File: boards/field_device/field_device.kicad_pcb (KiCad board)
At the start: 4 copper layers, 35 x 43.9 mm, 54 parts, among them J1 Conn_01x05_Pin, J2 Conn_01x02_Pin, SW1 SW_SPST, U1 CHT20MEMS, U2 STM32C011F6Px, U3 SPA06-003, U4 CN3163, U6 SX1262IMLTRT, U7 TPS63900, Y1 Crystal_GND24

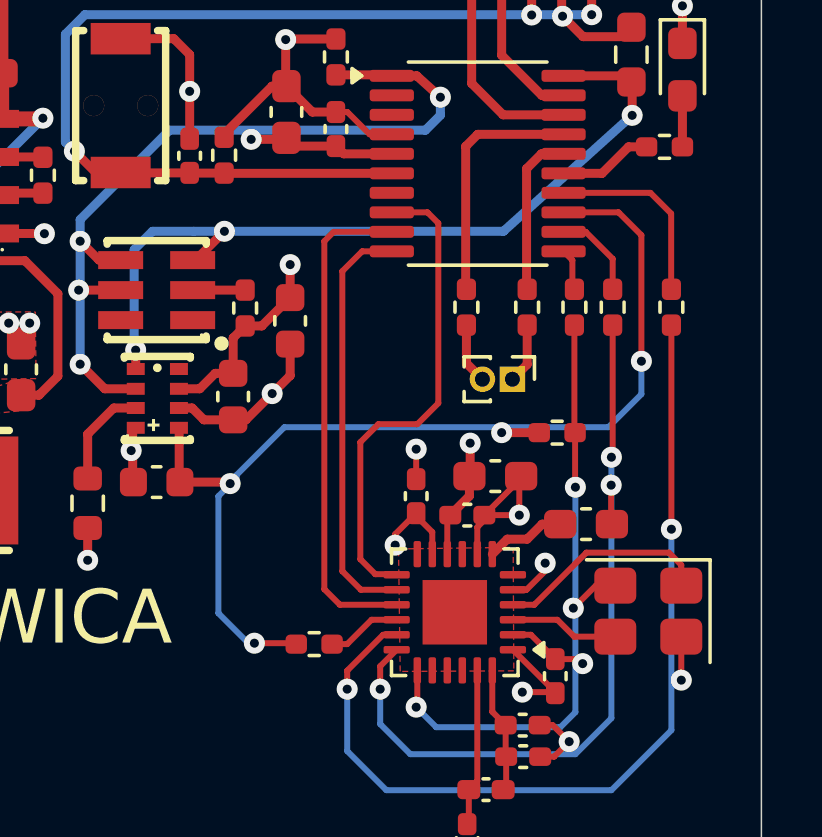
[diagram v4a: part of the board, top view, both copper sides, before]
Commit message: move resistors closer to pins
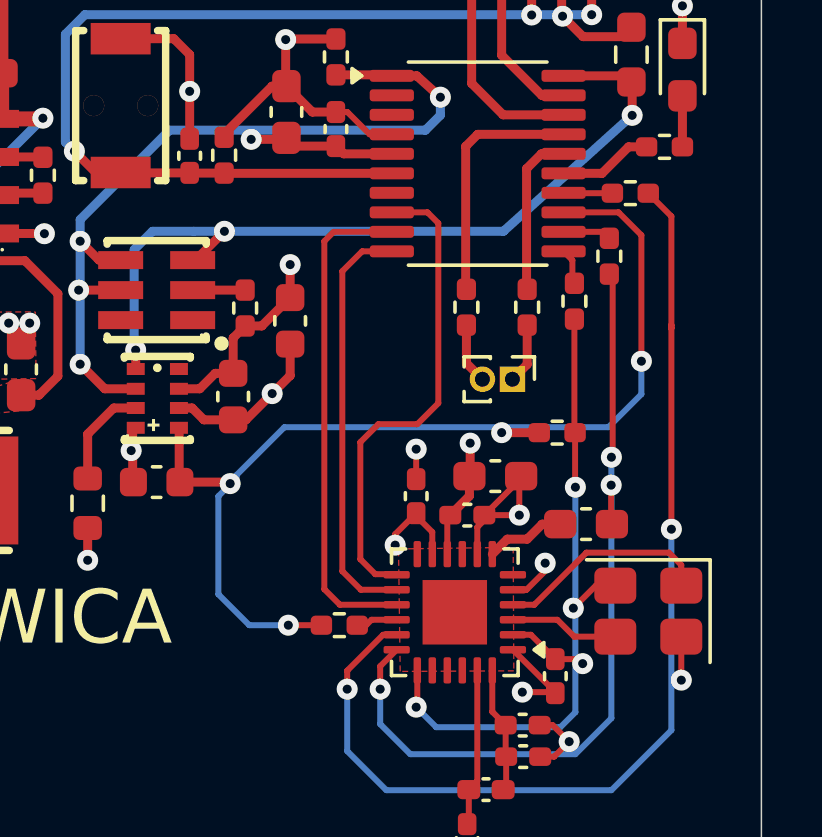
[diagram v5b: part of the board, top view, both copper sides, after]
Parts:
- moved R8 4.04 mm to (150.6, 39.1), turned to 0 degrees
- moved R6 1.70 mm to (149.9, 41.2)
- moved R7 1.05 mm to (140.9, 53.5)
- moved R5 0.20 mm to (148.7, 42.7)
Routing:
- net /MCU/MCU_MOSI: track 6.40 -> 1.63 mm
- net /MCU/RF_MOSI: track 30.6 -> 35.3 mm
- net /MCU/RF_SCK: track 24.5 -> 26.3 mm
- net /MCU/MCU_SCK: track 3.02 -> 1.61 mm
- net /MCU/RF_MISO: track 2.51 -> 1.41 mm
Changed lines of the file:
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@@
 	(footprint "Resistor_SMD:R_0402_1005Metric_Pad0.72x0.64mm_HandSolder"
 		(layer "F.Cu")
-		(at 150.011432 42.9 -90)
+		(at 149.9 41.2 -90)
 		(descr "Resistor SMD 0402 (1005 Metric), square (rectangular) end terminal, IPC-7351 nominal with elongated pad for handsoldering. (Body size source: IPC-SM-782 page 72, https://www.pcb-3d.com/wordpress/wp-content/uploads/ipc-sm-782a_amendment_1_and_2.pdf)")
 		(tags "resistor handsolder")
@@
 	(footprint "Resistor_SMD:R_0402_1005Metric_Pad0.72x0.64mm_HandSolder"
 		(layer "F.Cu")
-		(at 151.969091 42.9 -90)
+		(at 150.6 39.1)
 		(descr "Resistor SMD 0402 (1005 Metric), square (rectangular) end terminal, IPC-7351 nominal with elongated pad for handsoldering. (Body size source: IPC-SM-782 page 72, https://www.pcb-3d.com/wordpress/wp-content/uploads/ipc-sm-782a_amendment_1_and_2.pdf)")
 		(tags "resistor handsolder")
 		(property "Reference" "R8"
-			(at 0 -1.17 90)
+			(at 0 -1.17 0)
 			(layer "F.SilkS")
 			(hide yes)
@@
 		)
 		(property "Value" "22R"
-			(at 0 1.17 90)
+			(at 0 1.17 0)
 			(layer "F.Fab")
 			(effects
@@
 		)
 		(property "Datasheet" ""
-			(at 0 0 90)
+			(at 0 0 0)
 			(layer "F.Fab")
 			(hide yes)
@@
 		)
 		(property "Description" "Resistor"
-			(at 0 0 90)
+			(at 0 0 0)
 			(layer "F.Fab")
 			(hide yes)
@@
 		(duplicate_pad_numbers_are_jumpers no)
 		(fp_line
-			(start -0.167621 0.380001)
-			(end 0.167621 0.380001)
+			(start -0.167621 -0.380001)
+			(end 0.167621 -0.380001)
 			(stroke
 				(width 0.12)
@@
 		)
 		(fp_line
-			(start -0.167621 -0.380001)
-			(end 0.167621 -0.380001)
+			(start -0.167621 0.380001)
+			(end 0.167621 0.380001)
 			(stroke
 				(width 0.12)
@@
 		)
 		(fp_text user "${REFERENCE}"
-			(at 0 0 90)
+			(at 0 0 0)
 			(layer "F.Fab")
 			(effects
@@
 		)
 		(pad "1" smd roundrect
-			(at -0.5975 0 270)
+			(at -0.5975 0)
 			(size 0.715 0.64)
 			(layers "F.Cu" "F.Mask" "F.Paste")
@@
 		)
 		(pad "2" smd roundrect
-			(at 0.5975 0 270)
+			(at 0.5975 0)
 			(size 0.715 0.64)
 			(layers "F.Cu" "F.Mask" "F.Paste")
@@
 	(footprint "Resistor_SMD:R_0402_1005Metric_Pad0.72x0.64mm_HandSolder"
 		(layer "F.Cu")
-		(at 140.061432 54.13125)
+		(at 140.9 53.5)
 		(descr "Resistor SMD 0402 (1005 Metric), square (rectangular) end terminal, IPC-7351 nominal with elongated pad for handsoldering. (Body size source: IPC-SM-782 page 72, https://www.pcb-3d.com/wordpress/wp-content/uploads/ipc-sm-782a_amendment_1_and_2.pdf)")
 		(tags "resistor handsolder")
@@
 	(footprint "Resistor_SMD:R_0402_1005Metric_Pad0.72x0.64mm_HandSolder"
 		(layer "F.Cu")
-		(at 148.736432 42.9 -90)
+		(at 148.736432 42.7 -90)
 		(descr "Resistor SMD 0402 (1005 Metric), square (rectangular) end terminal, IPC-7351 nominal with elongated pad for handsoldering. (Body size source: IPC-SM-782 page 72, https://www.pcb-3d.com/wordpress/wp-content/uploads/ipc-sm-782a_amendment_1_and_2.pdf)")
 		(tags "resistor handsolder")
@@
 	)
 	(segment
-		(start 150.011432 41.287501)
-		(end 150.011432 42.3025)
+		(start 149.6855 40.388)
+		(end 148.374432 40.388)
 		(width 0.2)
 		(layer "F.Cu")
@@
 	)
 	(segment
-		(start 148.374432 40.388)
-		(end 149.111931 40.388)
+		(start 149.9 40.6025)
+		(end 149.6855 40.388)
 		(width 0.2)
 		(layer "F.Cu")
@@
 	)
 	(segment
-		(start 149.111931 40.388)
-		(end 150.011432 41.287501)
-		(width 0.2)
-		(layer "F.Cu")
-		(net "/MCU/MCU_SCK")
-	)
-	(segment
-		(start 150.011432 47.857659)
-		(end 149.969091 47.9)
+		(start 149.9 41.7975)
+		(end 150.011432 41.908932)
 		(width 0.2)
 		(layer "F.Cu")
@@
 	)
 	(segment
-		(start 150.011432 43.4975)
+		(start 142.261432 55.63125)
+		(end 142.261432 55.73125)
+		(width 0.2)
+		(layer "F.Cu")
+		(net "/MCU/RF_SCK")
+	)
+	(segment
+		(start 150.011432 41.908932)
 		(end 150.011432 47.857659)
 		(width 0.2)
@@
 	)
 	(segment
-		(start 142.261432 55.63125)
-		(end 142.261432 55.73125)
+		(start 150.011432 47.857659)
+		(end 149.969091 47.9)
 		(width 0.2)
 		(layer "F.Cu")
@@
 	)
 	(segment
-		(start 148.669091 41.332659)
-		(end 148.669091 42.235159)
+		(start 148.374432 41.038)
+		(end 148.669091 41.332659)
 		(width 0.2)
 		(layer "F.Cu")
@@
 	)
 	(segment
-		(start 148.669091 42.235159)
-		(end 148.736432 42.3025)
+		(start 148.669091 41.332659)
+		(end 148.669091 42.035159)
 		(width 0.2)
 		(layer "F.Cu")
@@
 	)
 	(segment
-		(start 148.374432 41.038)
-		(end 148.669091 41.332659)
+		(start 148.669091 42.035159)
+		(end 148.736432 42.1025)
 		(width 0.2)
 		(layer "F.Cu")
@@
 	)
 	(segment
-		(start 150.207091 39.738)
-		(end 150.969091 40.5)
-		(width 0.2)
-		(layer "F.Cu")
-		(net "/MCU/MCU_MISO")
-	)
-	(segment
-		(start 148.374432 39.738)
-		(end 150.207091 39.738)
+		(start 140.3025 53.5)
+		(end 139.2 53.5)
 		(width 0.2)
 		(layer "F.Cu")
@@
 	)
 	(segment
-		(start 138.069091 54.1)
-		(end 139.432682 54.1)
+		(start 150.207091 39.738)
+		(end 150.969091 40.5)
 		(width 0.2)
 		(layer "F.Cu")
@@
 	)
 	(segment
-		(start 139.432682 54.1)
-		(end 139.463932 54.13125)
+		(start 148.374432 39.738)
+		(end 150.207091 39.738)
 		(width 0.2)
 		(layer "F.Cu")
@@
 	)
 	(via
-		(at 138.069091 54.1)
+		(at 139.2 53.5)
 		(size 0.7)
 		(drill 0.3)
@@
 	)
 	(segment
-		(start 139.069091 46.9)
-		(end 137.469091 48.5)
+		(start 137.469091 48.5)
+		(end 139.069091 46.9)
 		(width 0.2)
 		(layer "B.Cu")
@@
 	)
 	(segment
-		(start 150.969091 44.7)
-		(end 150.969091 45.8)
+		(start 137.469091 48.6)
+		(end 137.469091 48.5)
 		(width 0.2)
 		(layer "B.Cu")
@@
 	)
 	(segment
-		(start 136.869091 53.1)
-		(end 137.869091 54.1)
+		(start 136.869091 52.469091)
+		(end 136.869091 49.2)
 		(width 0.2)
 		(layer "B.Cu")
@@
 	(segment
 		(start 136.869091 49.2)
-		(end 136.869091 53.1)
+		(end 137.469091 48.6)
 		(width 0.2)
 		(layer "B.Cu")
@@
 	(segment
 		(start 149.869091 46.9)
-		(end 139.069091 46.9)
+		(end 150.969091 45.8)
 		(width 0.2)
 		(layer "B.Cu")
@@
 	)
 	(segment
-		(start 137.469091 48.5)
-		(end 137.469091 48.6)
+		(start 139.2 53.5)
+		(end 137.9 53.5)
 		(width 0.2)
 		(layer "B.Cu")
@@
 	)
 	(segment
-		(start 150.969091 45.8)
+		(start 139.069091 46.9)
 		(end 149.869091 46.9)
 		(width 0.2)
@@
 	)
 	(segment
-		(start 137.869091 54.1)
-		(end 138.069091 54.1)
+		(start 137.9 53.5)
+		(end 136.869091 52.469091)
 		(width 0.2)
 		(layer "B.Cu")
@@
 	)
 	(segment
-		(start 137.469091 48.6)
-		(end 136.869091 49.2)
+		(start 150.969091 45.8)
+		(end 150.969091 44.7)
 		(width 0.2)
 		(layer "B.Cu")
@@
 	)
 	(segment
-		(start 151.961432 42.294841)
-		(end 151.969091 42.3025)
+		(start 150.0025 39.1)
+		(end 148.386432 39.1)
 		(width 0.2)
 		(layer "F.Cu")
@@
 	)
 	(segment
-		(start 151.961432 39.78)
-		(end 151.961432 42.294841)
-		(width 0.2)
-		(layer "F.Cu")
-		(net "/MCU/MCU_MOSI")
-	)
-	(segment
-		(start 151.269432 39.088)
-		(end 151.961432 39.78)
-		(width 0.2)
-		(layer "F.Cu")
-		(net "/MCU/MCU_MOSI")
-	)
-	(segment
-		(start 148.374432 39.088)
-		(end 151.269432 39.088)
+		(start 148.386432 39.1)
+		(end 148.374432 39.088)
 		(width 0.2)
 		(layer "F.Cu")
@@
 	)
 	(segment
+		(start 151.1975 39.1)
+		(end 151.969091 39.871591)
+		(width 0.2)
+		(layer "F.Cu")
+		(net "/MCU/RF_MOSI")
+	)
+	(segment
 		(start 142.359545 53.81875)
 		(end 141.161432 55.016863)
@@
 	)
 	(segment
+		(start 151.969091 39.871591)
+		(end 151.969091 43.4975)
+		(width 0.2)
+		(layer "F.Cu")
+		(net "/MCU/RF_MOSI")
+	)
+	(segment
 		(start 151.969091 43.4975)
 		(end 151.969091 43.5975)
@@
 	)
 	(segment
-		(start 141.973932 53.31875)
-		(end 141.161432 54.13125)
+		(start 142.811431 53.31875)
+		(end 141.973932 53.31875)
 		(width 0.2)
 		(layer "F.Cu")
@@
 	)
 	(segment
-		(start 141.161432 54.13125)
-		(end 140.658932 54.13125)
+		(start 141.973932 53.31875)
+		(end 141.792682 53.5)
 		(width 0.2)
 		(layer "F.Cu")
@@
 	)
 	(segment
-		(start 142.811431 53.31875)
-		(end 141.973932 53.31875)
+		(start 141.792682 53.5)
+		(end 141.4975 53.5)
 		(width 0.2)
 		(layer "F.Cu")
@@
 	)
 	(segment
-		(start 148.758932 48.889841)
-		(end 148.769091 48.9)
+		(start 148.736432 47.05875)
+		(end 148.758932 47.08125)
 		(width 0.2)
 		(layer "F.Cu")
@@
 	)
 	(segment
-		(start 148.736432 47.05875)
-		(end 148.758932 47.08125)
+		(start 148.758932 48.889841)
+		(end 148.769091 48.9)
 		(width 0.2)
 		(layer "F.Cu")
@@
 	)
 	(segment
-		(start 143.498931 55.00625)
-		(end 143.498931 56.193751)
+		(start 148.736432 43.2975)
+		(end 148.736432 47.05875)
 		(width 0.2)
 		(layer "F.Cu")
@@
 	)
 	(segment
-		(start 148.736432 43.4975)
-		(end 148.736432 47.05875)
+		(start 143.498931 55.00625)
+		(end 143.498931 56.193751)
 		(width 0.2)
 		(layer "F.Cu")

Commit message: rrev 4
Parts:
- removed L3: L_Series, Inductor_SMD:L_0402_1005Metric_Pad0.77x0.64mm_HandSolder
- added AE1: Antenna, custom:TI DN023 868-955MHz Antenna, F.Cu at (58.1, 70.7)
- added R17: 0, Resistor_SMD:R_0402_1005Metric_Pad0.72x0.64mm_HandSolder, F.Cu at (51.1, 49.4)
- added R18: 0603WAF3601T5E, Resistor_SMD:R_0603_1608Metric, F.Cu at (31.1, 30.5)
- C1: value 10u -> 10uF; footprint Capacitor_SMD:C_0603_1608Metric -> Capacitor_SMD:C_0603_1608Metric_Pad1.08x0.95mm_HandSolder
- C10: value 22u -> 22uF
- C2, C4: value 100n -> 100nF
- C3, C7, C8, C9: value 10u -> 10uF
- C5, C6: value 100n -> 100nF; footprint Capacitor_SMD:C_0603_1608Metric -> Capacitor_SMD:C_0402_1005Metric_Pad0.74x0.62mm_HandSolder
- D1: value STATUS -> KT-0603R
- D2: value ORANGE -> KT-0603R
- D3: value GREEN -> KT-0603R
- J1: value Conn_01x05_Pin -> ~; footprint Connector_PinHeader_1.00mm:PinHeader_1x05_P1.00mm_Vertical -> Connector_PinHeader_2.54mm:PinHeader_1x05_P2.54mm_Vertical
- J2: value Conn_01x02_Pin -> ~; footprint Connector_PinHeader_1.00mm:PinHeader_1x02_P1.00mm_Vertical -> Connector_PinHeader_2.54mm:PinHeader_1x02_P2.54mm_Vertical
- L1: value 2u2 -> 2.2uH Ceaiya CR4018-2R2M; footprint UnEasy-LCSC:IND-SMD_L4.0-W4.0_B -> UnEasy-LCSC:IND-SMD_L4.0-W4.0
- R13: value 10k? -> 10k; footprint Resistor_SMD:R_0603_1608Metric -> Resistor_SMD:R_0402_1005Metric_Pad0.72x0.64mm_HandSolder
- R14: value 1k5 -> 1k
- R15: footprint Capacitor_SMD:C_0603_1608Metric_Pad1.08x0.95mm_HandSolder -> Resistor_SMD:R_0402_1005Metric_Pad0.72x0.64mm_HandSolder
- R16: value 36k5 -> 0603WAF3302T5E; footprint Resistor_SMD:R_0402_1005Metric_Pad0.72x0.64mm_HandSolder -> Resistor_SMD:R_0603_1608Metric
- R3: footprint Resistor_SMD:R_0603_1608Metric_Pad0.98x0.95mm_HandSolder -> Resistor_SMD:R_0402_1005Metric_Pad0.72x0.64mm_HandSolder
- R4: value 10k? -> 10k
- SW1: value SW_SPST -> TS-1088-AR02016; footprint UnEasy-LCSC:KEY-SMD_L3.9-W3.0-LS5.0-EH -> UnEasy-LCSC:SW-SMD_L3.9-W3.0-P4.45
- U2: value STM32C011F6Px -> STM32C051F8P6
- U6: footprint Package_DFN_QFN:QFN-24-1EP_4x4mm_P0.5mm_EP2.15x2.15mm -> UnEasy-LCSC:QFN-24_L4.0-W4.0-P0.50-BL-EP2.6
- Y1: value Crystal_GND24 -> X322532MMB4SI; footprint Crystal:Crystal_SMD_3225-4Pin_3.2x2.5mm -> UnEasy-LCSC:CRYSTAL-SMD_4P-L3.2-W2.5-BL
- moved J2 130.2 mm to (20.0, 15.0)
- moved J1 99.3 mm to (47.4, 15.0)
- moved C21 98.2 mm to (49.4, 48.7), turned to 180 degrees
- moved BT1 97.7 mm to (28.5, 14.8)
- moved C10 95.7 mm to (30.3, 34.3)
- moved C9 95.7 mm to (35.2, 34.3)
- moved L1 95.7 mm to (32.8, 38.4)
- moved U7 95.7 mm to (32.7, 34.2)
- moved R13 95.5 mm to (38.3, 33.8)
- moved C2 95.4 mm to (41.5, 24.0)
- moved SW1 95.4 mm to (39.2, 22.4)
- moved R4 95.1 mm to (43.0, 24.0)
- moved U6 95.0 mm to (50.7, 39.4), turned to 90 degrees
- moved C1 95.0 mm to (45.2, 29.7)
- moved C18 95.0 mm to (53.0, 43.1)
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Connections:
- C22 pad 1: Net-(AE1-A) -> GND
- R16 pad 1: /power_source/regulator/CFG1 -> Net-(R16-Pad1)
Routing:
- net /MCU/LOG_MCU_TX_DEBUGGER_RX: track 2.01 -> 54.9 mm, vias 0 -> 1
- net /MCU/LOG_MCU_RX_DEBUGGER_TX: track 2.02 -> 48.8 mm, vias 0 -> 2
- net /power_source/regulator/Vin: track 26.2 -> 35.1 mm, vias 0 -> 2
- net GND: track 67.3 -> 75.4 mm
- net /MCU/SWDIO: track 7.43 -> 11.9 mm
- net /MCU/SWDCLK: track 5.61 -> 9.41 mm
- net /power_source/regulator/CFG1: track 1.44 -> 4.55 mm
- net /power_source/solar_pwr: track 18.6 -> 21.2 mm
- net +3.3V: track 38.7 -> 41.2 mm, vias 10 -> 9
- net Net-(R16-Pad1): track 0.00 -> 1.85 mm
- net Net-(D2-A): track 13.9 -> 15.5 mm
- net Net-(U3-CSB): track 3.44 -> 2.03 mm
- net Net-(AE1-A): track 1.11 -> 0.00 mm
- net /MCU/LOG_MCU_RX: track 8.20 -> 7.17 mm
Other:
- board size 35 x 43.9 mm -> 50 x 60 mm
- board text added: "3V3"
- board text added: "A"
- board text added: "All the words I left unsaid that day"
- board text added: "BATTERY"
- board text added: "C"
- board text added: "DBG_RX"
- board text added: "DBG_TX"
- board text added: "Didn't you see the news today?"
- board text added: "GND"
- board text added: "Goofy"
- board text added: "I"
- board text added: "I heard they said it looked like rain"
- board text added: "NRST"
- board text added: "Revision 4"
- board text added: "SOLAR"
- board text added: "SWCLK"
- board text added: "SWDIO"
- board text added: "Stained the sidewalk drop-by-drop"
- board text added: "W"
- board text added: "eather"
- board text added: "nformation"
- board text added: "ollection"
- board text added: "rray"
- board text added: "with gray."
- board text removed: "Goofy WICA"

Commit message: test
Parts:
- moved Y1 0.24 mm to (57.4, 39.3)
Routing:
- net /MCU/LOG_MCU_TX_DEBUGGER_RX: track 54.9 -> 55.4 mm

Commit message: i dont even know
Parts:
- L1: value 2.2uH Ceaiya CR4018-2R2M -> CR4018-2R2M
- moved Y1 1.56 mm to (58.6, 40.4)
- moved C22 0.38 mm to (53.1, 50.0)
- moved R17 0.35 mm to (51.5, 49.4)
- moved C20 0.33 mm to (51.5, 47.0)
- moved C21 0.29 mm to (49.7, 48.8)
- moved AE1 0.28 mm to (58.4, 70.7)
- moved L2 0.28 mm to (52.0, 45.3)
- moved C19 0.20 mm to (53.2, 44.2)
- moved C18 0.20 mm to (53.2, 43.1)
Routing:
- net GND: track 75.4 -> 73.3 mm, vias 24 -> 23
- net /lora_module/XTA: track 3.65 -> 5.53 mm
- net /lora_module/XTB: track 7.19 -> 8.98 mm
- net Net-(D2-A): track 15.5 -> 14.1 mm
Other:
- board text removed: "Revision 4"
